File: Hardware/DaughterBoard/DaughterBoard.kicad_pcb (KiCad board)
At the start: 2 copper layers, 145 x 160 mm, 50 parts, among them J1 CARTDRIGE, J2 ROM, J3 ISA00, J4 ISA10, J5 AUDIO_OUT, J6 VGA_OUT, J7 ISA01, J8 ISA11, SW1 RESET, U1 ATmega328P-PU, U2 ATmega1284P-PU, U4 ATmega328P-PU, U5 HM62256BLP, U6 74LS365, X1 ACO-20MHz, Y1 16MHz

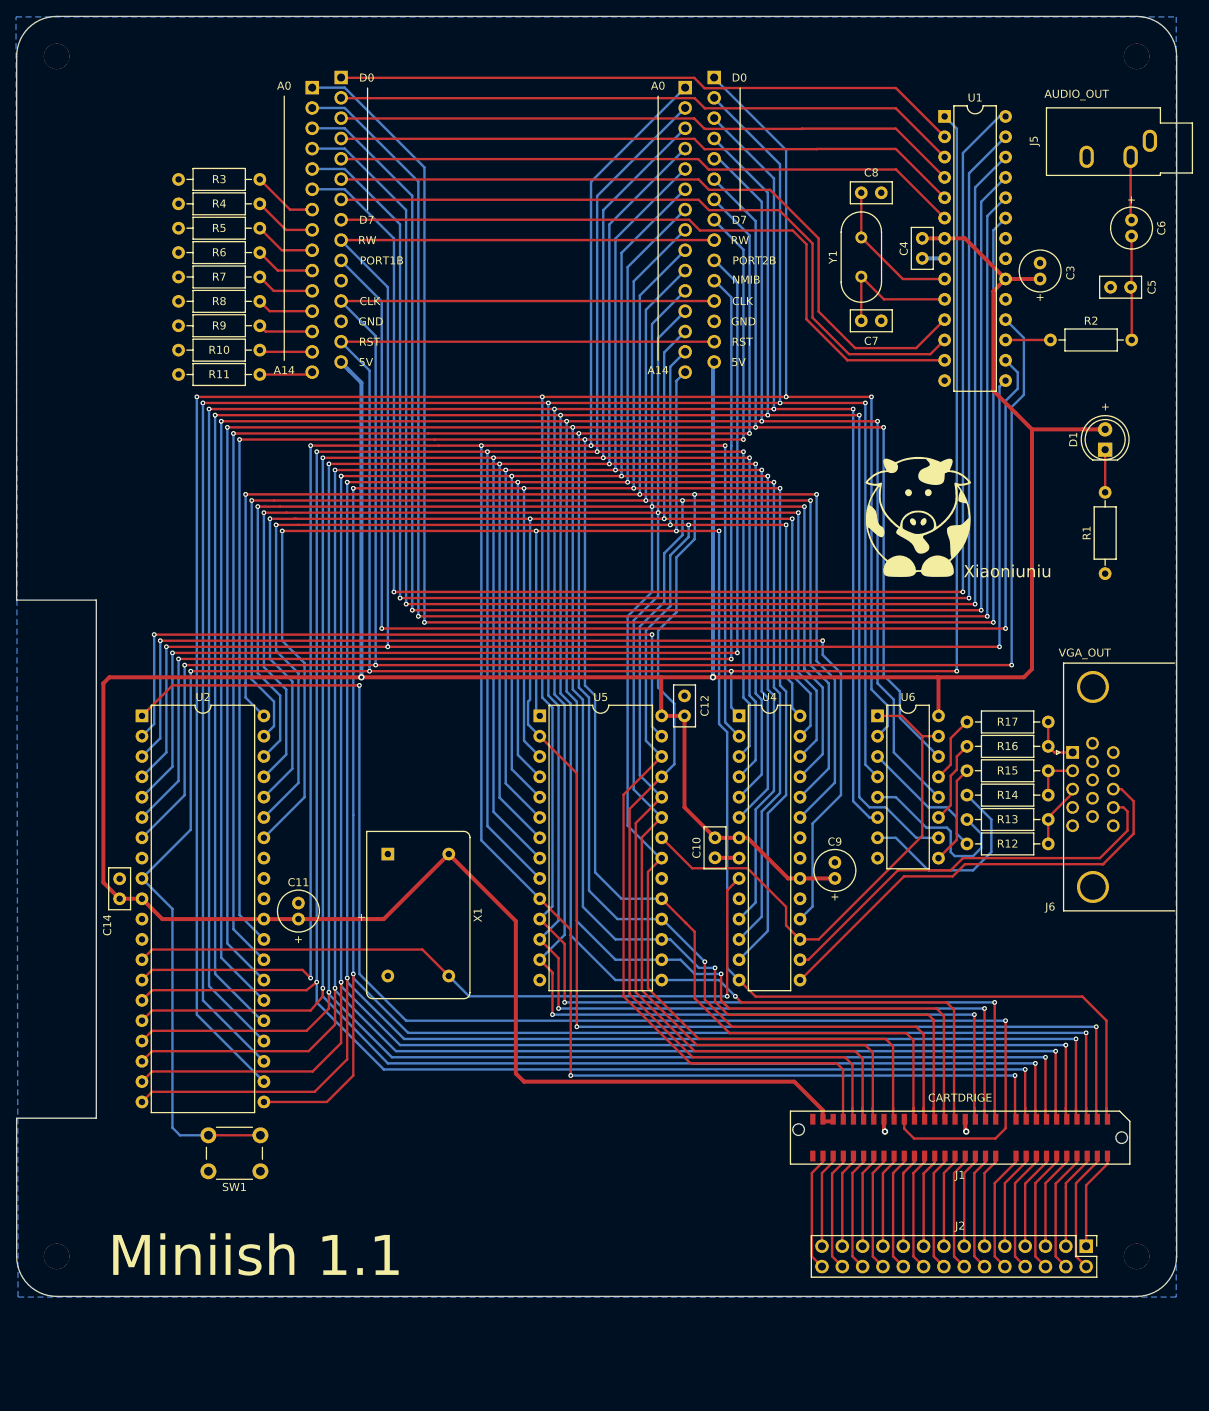
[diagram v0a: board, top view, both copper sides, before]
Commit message: implement graphic loading from ROM
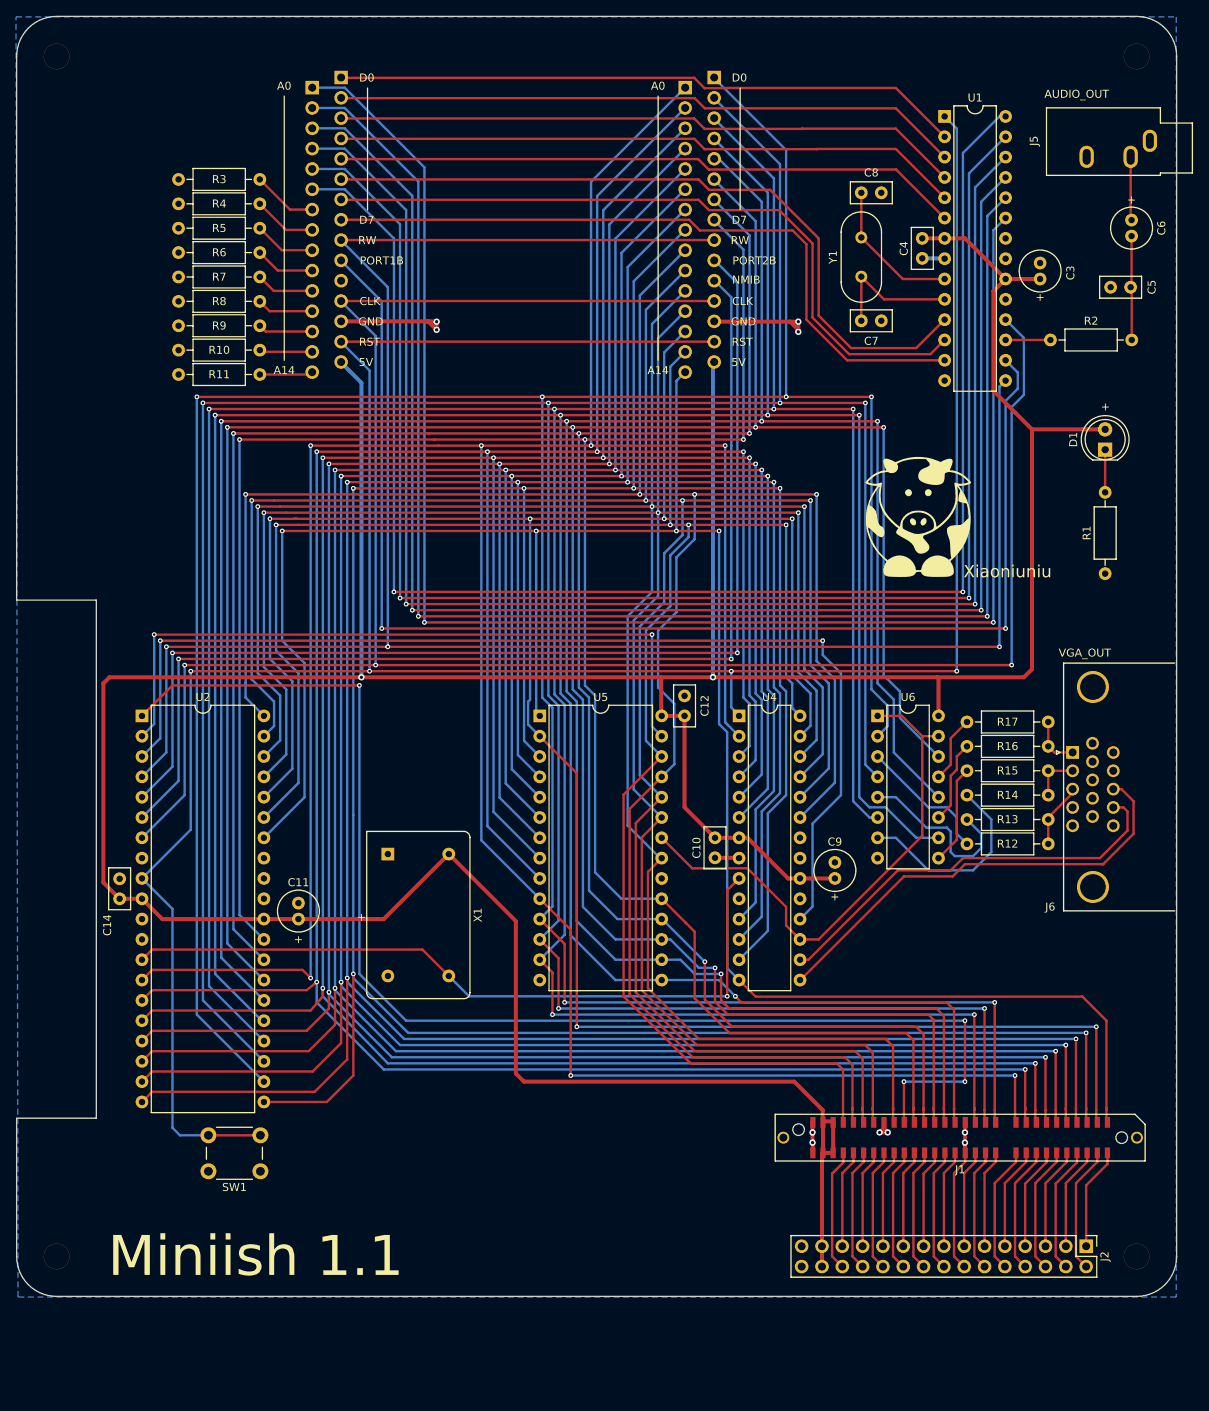
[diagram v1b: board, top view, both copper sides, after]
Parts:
- J1: footprint Connector_PCBEdge:Samtec_MECF-30-02-L-DV_2x30_P1.27mm_Polarized_Socket_Horizontal -> Connector_PCBEdge:Samtec_MECF-30-01-L-DV-WT_2x30_P1.27mm_Polarized_Socket_Horizontal
- J2: footprint Connector_PinHeader_2.54mm:PinHeader_2x14_P2.54mm_Vertical -> Connector_PinHeader_2.54mm:PinHeader_2x15_P2.54mm_Vertical
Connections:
- J1 pad 30: Net-(J1-Pad30) -> GND
- J1 pad 56: Net-(J1-Pad56) -> +5V
- J1 pad 58: Net-(J1-Pad58) -> +5V
- J1 pad 59: no_connect_107 -> GND
- J1 pad 60: no_connect_108 -> GND
- J2 pad 14: Net-(J1-Pad30) -> GND
- J2 pad 27: Net-(J1-Pad56) -> +5V
- J2 pad 28: Net-(J1-Pad58) -> +5V
- J3 pad 11: no_connect_109 -> no_connect_104
- J6 pad 11: no_connect_110 -> no_connect_105
- J6 pad 12: no_connect_111 -> no_connect_106
- J6 pad 15: no_connect_112 -> no_connect_107
- J6 pad 4: no_connect_113 -> no_connect_108
- J6 pad 9: no_connect_114 -> no_connect_109
- U1 pad 14: no_connect_115 -> no_connect_110
- U1 pad 19: no_connect_116 -> no_connect_111
- U2 pad 12: no_connect_117 -> no_connect_112
- U2 pad 33: no_connect_118 -> no_connect_113
- U2 pad 8: no_connect_119 -> no_connect_114
- U4 pad 10: no_connect_120 -> no_connect_115
- U4 pad 19: no_connect_121 -> no_connect_116
- X1 pad 1: no_connect_122 -> no_connect_117
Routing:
- net GND: track 8.45 -> 60.3 mm, vias 2 -> 10
- net +5V: track 468.3 -> 491.5 mm
- net Net-(J1-Pad58): track 14.9 -> 0.00 mm
- net Net-(J1-Pad30): track 14.9 -> 0.00 mm
- net ROMB: track 176.5 -> 163.5 mm, vias 2 -> 4
- net Net-(J1-Pad56): track 11.9 -> 0.00 mm

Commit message: Implement APU and fix schematics
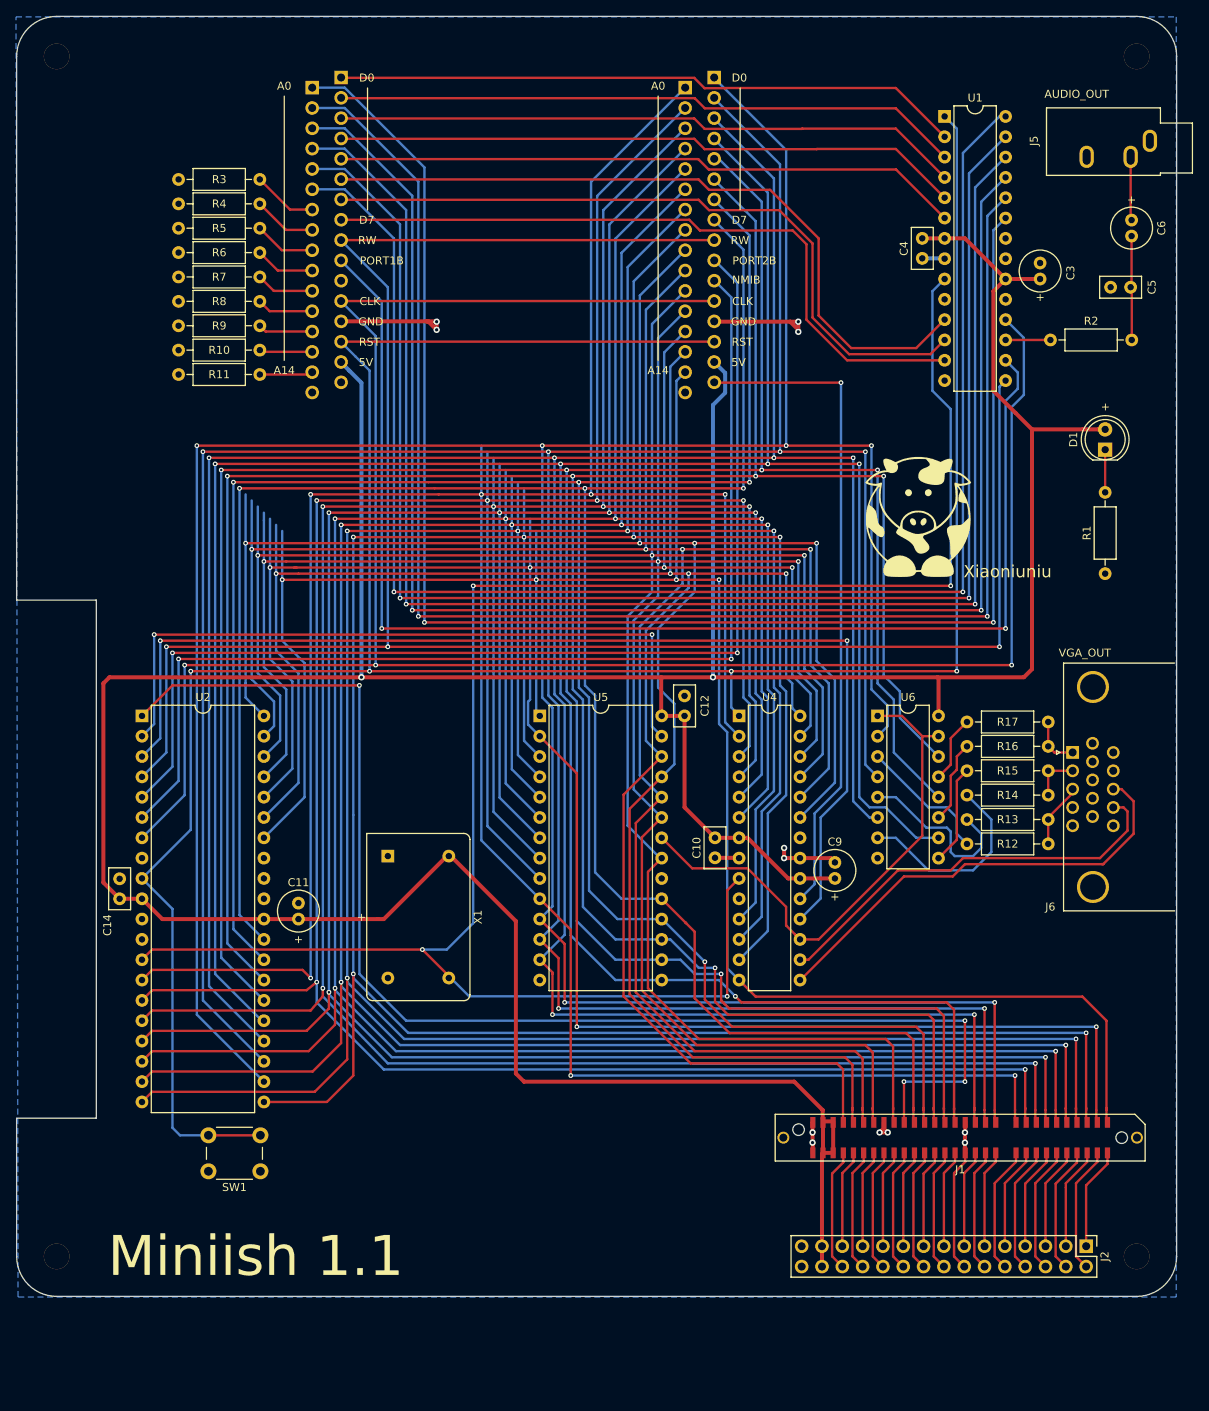
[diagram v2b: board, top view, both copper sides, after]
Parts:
- removed C7, C8: 22pF, Capacitor_THT:C_Disc_D5.0mm_W2.5mm_P2.50mm
- removed Y1: 16MHz, Crystal:Crystal_HC18-U_Vertical
- J3, J4, J7, J8: footprint Connector_PinHeader_2.54mm:PinHeader_1x15_P2.54mm_Vertical -> Connector_PinHeader_2.54mm:PinHeader_1x16_P2.54mm_Vertical
- R12, R14, R16: value 680 -> 1.5K
- R13, R15, R17: value 1.5K -> 680
- moved X1 0.25 mm to (71.4, 131.1)
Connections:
- J3 pad 11: no_connect_104 -> no_connect_103
- U1 pad 10: XTAL2 -> no_connect_110
- U1 pad 14: no_connect_110 -> no_connect_111
- U1 pad 19: no_connect_111 -> no_connect_112
- U1 pad 9: XTAL1 -> CLOCK2
- U2 pad 12: no_connect_112 -> no_connect_113
- U2 pad 33: no_connect_113 -> no_connect_114
- U2 pad 8: no_connect_114 -> no_connect_115
- U4 pad 10: no_connect_115 -> no_connect_116
- U4 pad 19: no_connect_116 -> /RDYB
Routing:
- net CLOCK2: track 92.0 -> 240.9 mm, vias 1 -> 4
- net /RDYB: track 0.00 -> 82.5 mm, vias 0 -> 1
- net XTAL1: track 18.2 -> 0.00 mm
- net XTAL2: track 17.1 -> 0.00 mm
- net /D2: track 399.9 -> 386.9 mm
- net /D5: track 355.6 -> 343.4 mm
- net /D3: track 387.1 -> 374.9 mm
- net /D1: track 402.5 -> 390.3 mm
- net /D0: track 407.4 -> 395.2 mm
- net /D4: track 371.5 -> 359.3 mm
- net GND: track 60.3 -> 68.2 mm, vias 10 -> 12
- net /A0: track 371.9 -> 365.6 mm
- net /D6: track 283.6 -> 277.5 mm
- net /A6: track 393.0 -> 386.9 mm
- net /A5: track 393.7 -> 387.6 mm
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
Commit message: Implement DMA and PCB ports
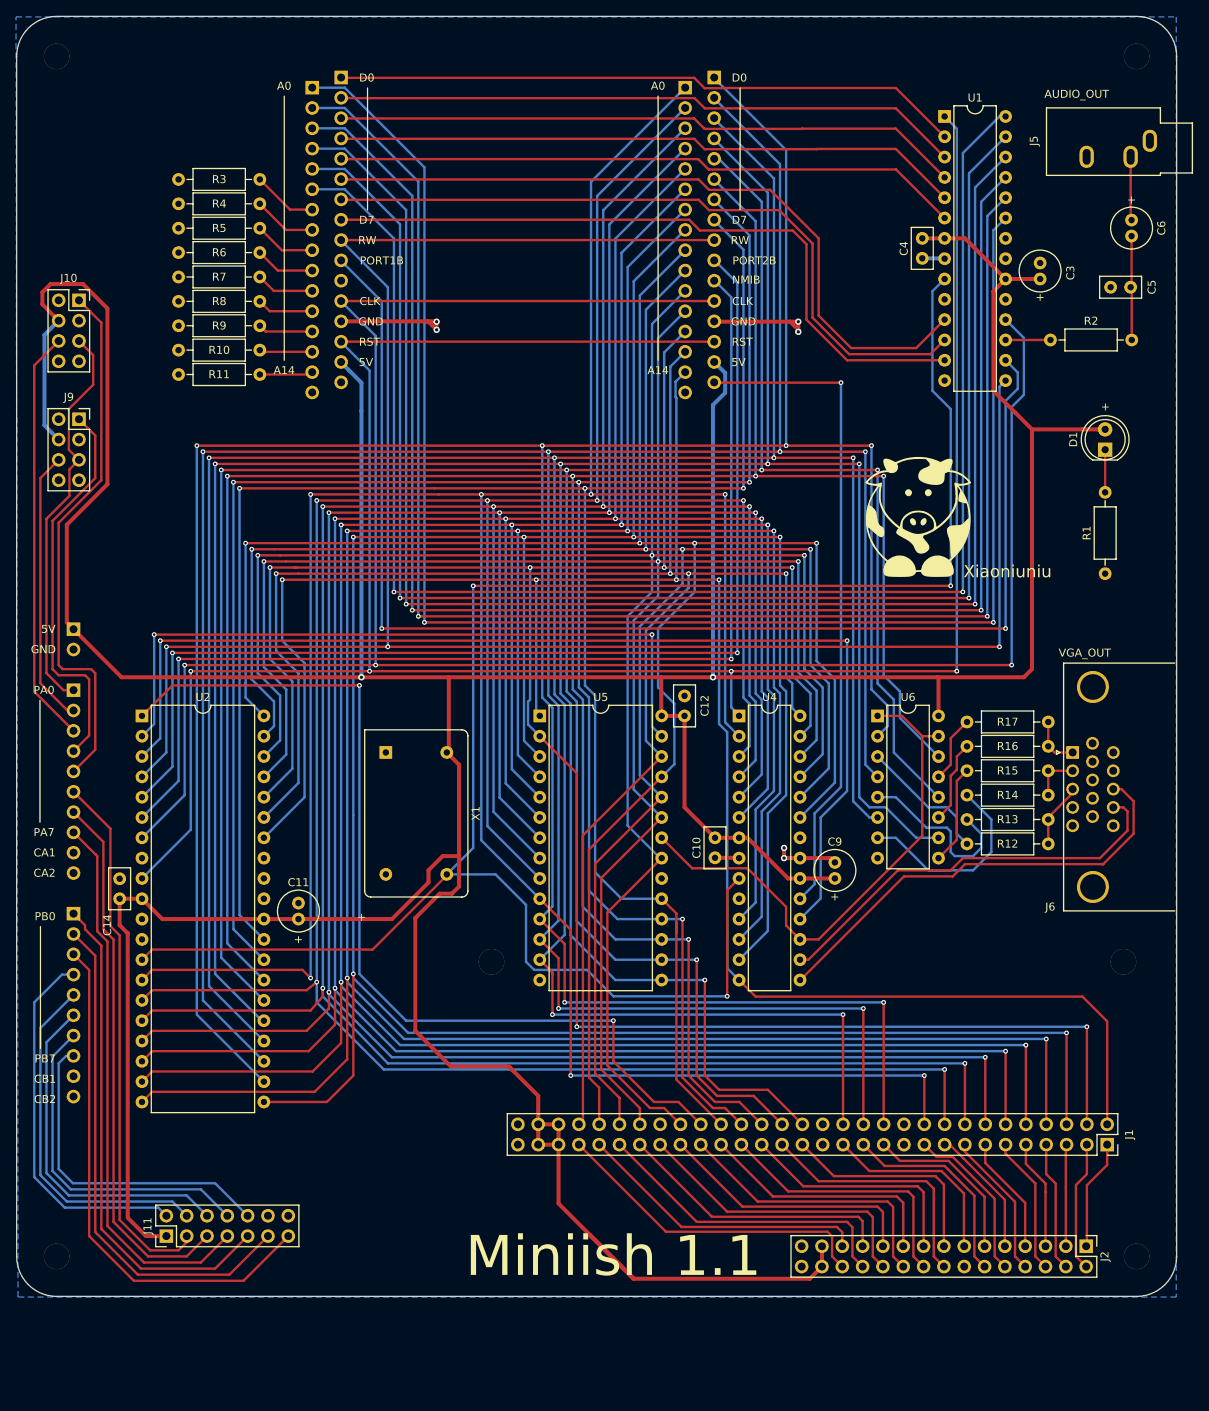
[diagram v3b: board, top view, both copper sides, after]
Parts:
- removed SW1: RESET, Button_Switch_THT:SW_PUSH_6mm_H5mm
- added H4: MountingHole_Pad, MountingHole:MountingHole_3.2mm_M3, F.Cu at (84.3, 144.3)
- added H4: MountingHole_Pad, MountingHole:MountingHole_3.2mm_M3, F.Cu at (163.3, 144.3)
- added J10: JOYPAD2, Connector_PinSocket_2.54mm:PinSocket_2x04_P2.54mm_Vertical, F.Cu at (32.8, 61.6)
- added J11: LCD, Connector_PinHeader_2.54mm:PinHeader_2x07_P2.54mm_Vertical, F.Cu at (43.7, 178.6)
- added J12: POWER, Connector_PinHeader_2.54mm:PinHeader_1x02_P2.54mm_Vertical, B.Cu at (32.1, 102.7)
- added J13: PA, Connector_PinHeader_2.54mm:PinHeader_1x10_P2.54mm_Vertical, B.Cu at (32.1, 110.3)
- added J14: PB, Connector_PinHeader_2.54mm:PinHeader_1x10_P2.54mm_Vertical, B.Cu at (32.1, 138.3)
- added J9: JOYPAD1, Connector_PinSocket_2.54mm:PinSocket_2x04_P2.54mm_Vertical, F.Cu at (32.8, 76.5)
- J1: footprint Connector_PCBEdge:Samtec_MECF-30-01-L-DV-WT_2x30_P1.27mm_Polarized_Socket_Horizontal -> Connector_PinSocket_2.54mm:PinSocket_2x30_P2.54mm_Vertical
- moved J1 18.4 mm to (161.3, 167.1), turned to -90 degrees
- moved X1 13.0 mm to (71.1, 118.1)
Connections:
- net no_connect_103 renamed no_connect_125
- net no_connect_104 renamed no_connect_126
- net no_connect_105 renamed no_connect_127
- net no_connect_106 renamed no_connect_128
- net no_connect_107 renamed no_connect_129
- net no_connect_108 renamed no_connect_130
- net no_connect_109 renamed no_connect_131
- net no_connect_110 renamed no_connect_133
- net no_connect_111 renamed no_connect_134
- net no_connect_112 renamed no_connect_135
- net no_connect_113 renamed no_connect_136
- net no_connect_114 renamed no_connect_137
- net no_connect_115 renamed no_connect_138
- net no_connect_116 renamed no_connect_139
- net no_connect_117 renamed no_connect_140
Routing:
- net +5V: track 492.6 -> 632.2 mm
- net LCD_EN: track 0.00 -> 69.2 mm
- net LCD_RW: track 0.00 -> 67.8 mm
- net JP_DATA2: track 0.00 -> 67.4 mm
- net LCD_RS: track 0.00 -> 67.0 mm
- net LCD_D2: track 0.00 -> 65.6 mm
- net LCD_D1: track 0.00 -> 64.2 mm
- net LCD_D0: track 0.00 -> 62.9 mm
- net JP_LATCH2: track 0.00 -> 52.0 mm
- net JP_CLOCK: track 0.00 -> 50.0 mm
- net JP_DATA1: track 0.00 -> 49.2 mm
- net LCD_D3: track 0.00 -> 46.7 mm
- net ROMB: track 163.5 -> 118.3 mm, vias 4 -> 2
- net LCD_D4: track 0.00 -> 44.6 mm
- net RESET: track 333.6 -> 289.4 mm
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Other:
- outline, holes or cut-outs redrawn
- board text added: "CA1"
- board text added: "CA2"
- board text added: "CB1"
- board text added: "CB2"
- board text added: "PA0"
- board text added: "PA7"
- board text added: "PB0"
- board text added: "PB7"
